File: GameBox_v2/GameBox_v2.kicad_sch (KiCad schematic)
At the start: 18 parts, among them J1 OLED, SW1 SW_left, SW2 SW_up, SW3 SW_down, SW4 SW_right, SW5 ON/OFF, U1 ATmega328P-P, U2 3.3V_boost_regulator, Y1 16MHz

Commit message: Rounded tracks and teardrops
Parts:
- SW5: footprint GameBox:SS12D10 -> GameBox:SS12D00
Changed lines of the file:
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@@
       (effects (font (size 1.27 1.27)) (justify right))
     )
-    (property "Footprint" "GameBox:SS12D10" (id 2) (at 123.19 35.56 0)
+    (property "Footprint" "GameBox:SS12D00" (id 2) (at 123.19 35.56 0)
       (effects (font (size 1.27 1.27)) hide)
     )
@@
     )
     (path "/15e1670d-9e79-4a5e-88ad-fbbb238a3e8a"
-      (reference "SW5") (unit 1) (value "ON/OFF") (footprint "GameBox:SS12D10")
+      (reference "SW5") (unit 1) (value "ON/OFF") (footprint "GameBox:SS12D00")
     )
     (path "/82782dc2-cb84-4d0c-b85e-b3903aca1e13"

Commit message: Footprint updates
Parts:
- SW5: footprint GameBox:SS12D00 -> GameBox:EG1218
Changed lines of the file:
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@@
       (effects (font (size 1.27 1.27)) (justify right))
     )
-    (property "Footprint" "GameBox:SS12D00" (id 2) (at 123.19 35.56 0)
+    (property "Footprint" "GameBox:EG1218" (id 2) (at 123.19 35.56 0)
       (effects (font (size 1.27 1.27)) hide)
     )
@@
     )
     (path "/15e1670d-9e79-4a5e-88ad-fbbb238a3e8a"
-      (reference "SW5") (unit 1) (value "ON/OFF") (footprint "GameBox:SS12D00")
+      (reference "SW5") (unit 1) (value "ON/OFF") (footprint "GameBox:EG1218")
     )
     (path "/82782dc2-cb84-4d0c-b85e-b3903aca1e13"

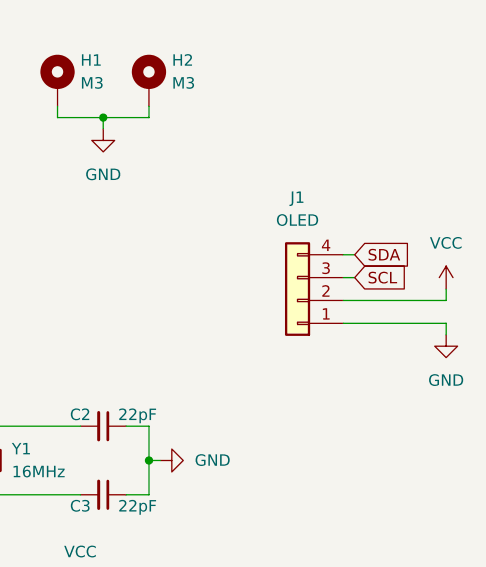
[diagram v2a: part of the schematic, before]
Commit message: fixed OLEDs
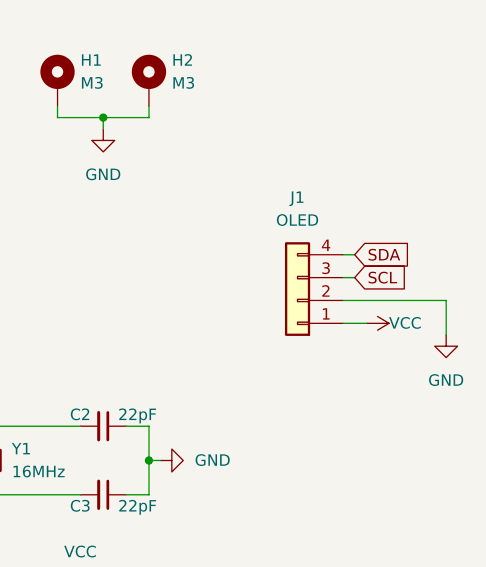
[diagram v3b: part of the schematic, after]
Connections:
- net GND: now also J1.2 (Pin_2); no longer J1.1 (Pin_1)
- net VCC: now also J1.1 (Pin_1); no longer J1.2 (Pin_2)
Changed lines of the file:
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@@
+    (stroke (width 0) (type default) (color 0 0 0 0))
+  )
+  (wire (pts (xy 209.55 85.09) (xy 209.55 88.9))
     (stroke (width 0) (type default) (color 0 0 0 0))
   )
@@
     (stroke (width 0) (type default) (color 0 0 0 0))
   )
-  (wire (pts (xy 198.12 87.63) (xy 209.55 87.63))
+  (wire (pts (xy 198.12 87.63) (xy 200.66 87.63))
     (stroke (width 0) (type default) (color 0 0 0 0))
   )
@@
     (stroke (width 0) (type default) (color 0 0 0 0))
   )
-  (wire (pts (xy 209.55 87.63) (xy 209.55 88.9))
-    (stroke (width 0) (type default) (color 0 0 0 0))
-  )
   (wire (pts (xy 125.73 73.66) (xy 128.27 73.66))
     (stroke (width 0) (type default) (color 0 0 0 0))
@@
     (stroke (width 0) (type default) (color 0 0 0 0))
   )
-  (wire (pts (xy 209.55 85.09) (xy 209.55 83.82))
-    (stroke (width 0) (type default) (color 0 0 0 0))
-  )
   (wire (pts (xy 152.4 106.68) (xy 157.48 106.68))
     (stroke (width 0) (type default) (color 0 0 0 0))
@@
     )
   )
-  (symbol (lib_id "power:VCC") (at 209.55 83.82 0) (unit 1)
-    (in_bom yes) (on_board yes) (fields_autoplaced)
-    (property "Reference" "#PWR06" (id 0) (at 209.55 87.63 0)
+  (symbol (lib_id "power:VCC") (at 200.66 87.63 270) (unit 1)
+    (in_bom yes) (on_board yes)
+    (property "Reference" "#PWR06" (id 0) (at 196.85 87.63 0)
       (effects (font (size 1.27 1.27)) hide)
     )
-    (property "Value" "VCC" (id 1) (at 209.55 78.74 0))
-    (property "Footprint" "" (id 2) (at 209.55 83.82 0)
+    (property "Value" "VCC" (id 1) (at 203.2 87.63 90)
+      (effects (font (size 1.27 1.27)) (justify left))
+    )
+    (property "Footprint" "" (id 2) (at 200.66 87.63 0)
       (effects (font (size 1.27 1.27)) hide)
     )
-    (property "Datasheet" "" (id 3) (at 209.55 83.82 0)
+    (property "Datasheet" "" (id 3) (at 200.66 87.63 0)
       (effects (font (size 1.27 1.27)) hide)
     )
